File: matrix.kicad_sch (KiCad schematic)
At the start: 43 parts

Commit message: Changed MCU to STM32, Redone footprints for USB, keyswitches, LEDS, and other things, and configured PCB Editor for general switch placement
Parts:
- D1, D10, D11, D12, D13, D14, D15, D16, D17, D18, D19, D2, D20, D3, D4, D5, D6, D7, D8, D9: footprint Diodes_SMD:D_SOD-123 -> Diode_SMD:D_SOD-123
- MX1, MX10, MX11, MX12, MX13, MX14, MX15, MX16, MX17, MX18, MX19, MX2, MX20, MX3, MX4, MX5, MX6, MX7, MX8, MX9: footprint (none) -> MX_Only:MXOnly-1U-NoLED
- MX21, MX22, MX23: footprint (none) -> MX_Only:MXOnly-2U-ReversedStabilizers-NoLED

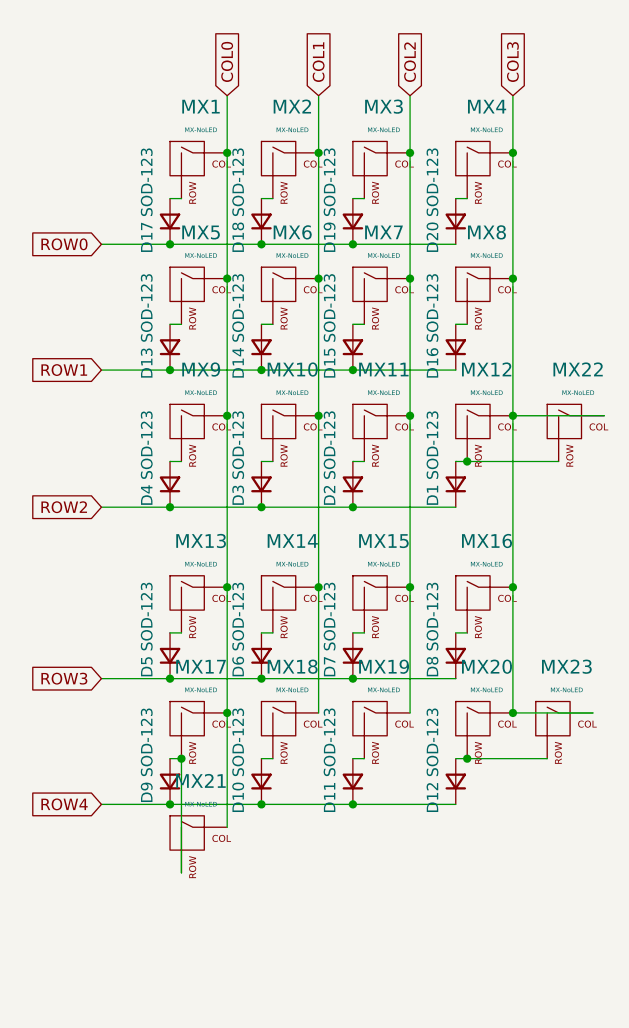
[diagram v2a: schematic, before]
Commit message: Placed Components and in the process of routing
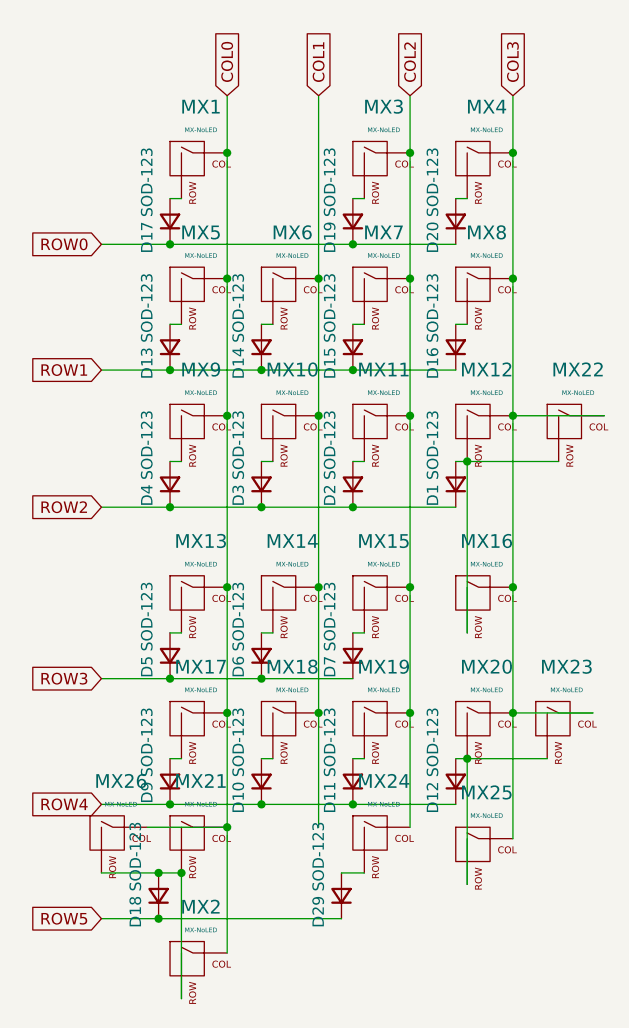
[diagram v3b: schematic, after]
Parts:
- removed D8: SOD-123, Diode_SMD:D_SOD-123, symbol Device:D_Small
- added D29: SOD-123, Diode_SMD:D_SOD-123, symbol Device:D_Small
- added MX24, MX25, MX26: MX-NoLED, MX_Only:MXOnly-1U-NoLED, symbol MX_Alps_Hybrid:MX-NoLED
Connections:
- net COL0: now also MX2.1 (COL), MX26.1 (COL)
- net COL1: no longer MX2.1 (COL)
- net COL2: now also MX24.1 (COL)
- net COL3: now also MX25.1 (COL)
- net ROW0: no longer D18.1 (K)
- net at D18.2 (A), MX2.2 (ROW): now also MX21.2 (ROW), MX26.2 (ROW)
- net at D12.2 (A), MX20.2 (ROW), MX23.2 (ROW): now also MX25.2 (ROW)
- net at D9.2 (A), MX17.2 (ROW): no longer MX21.2 (ROW)
- net at MX16.2 (ROW): now also D1.2 (A), MX12.2 (ROW), MX22.2 (ROW)
- new net: D29.2 (A), MX24.2 (ROW)
- new net ROW5: D18.1 (K), D29.1 (K)
